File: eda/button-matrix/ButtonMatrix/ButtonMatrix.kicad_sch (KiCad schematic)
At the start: 50 parts, among them J1 Conn_01x12, J2 Conn_01x12

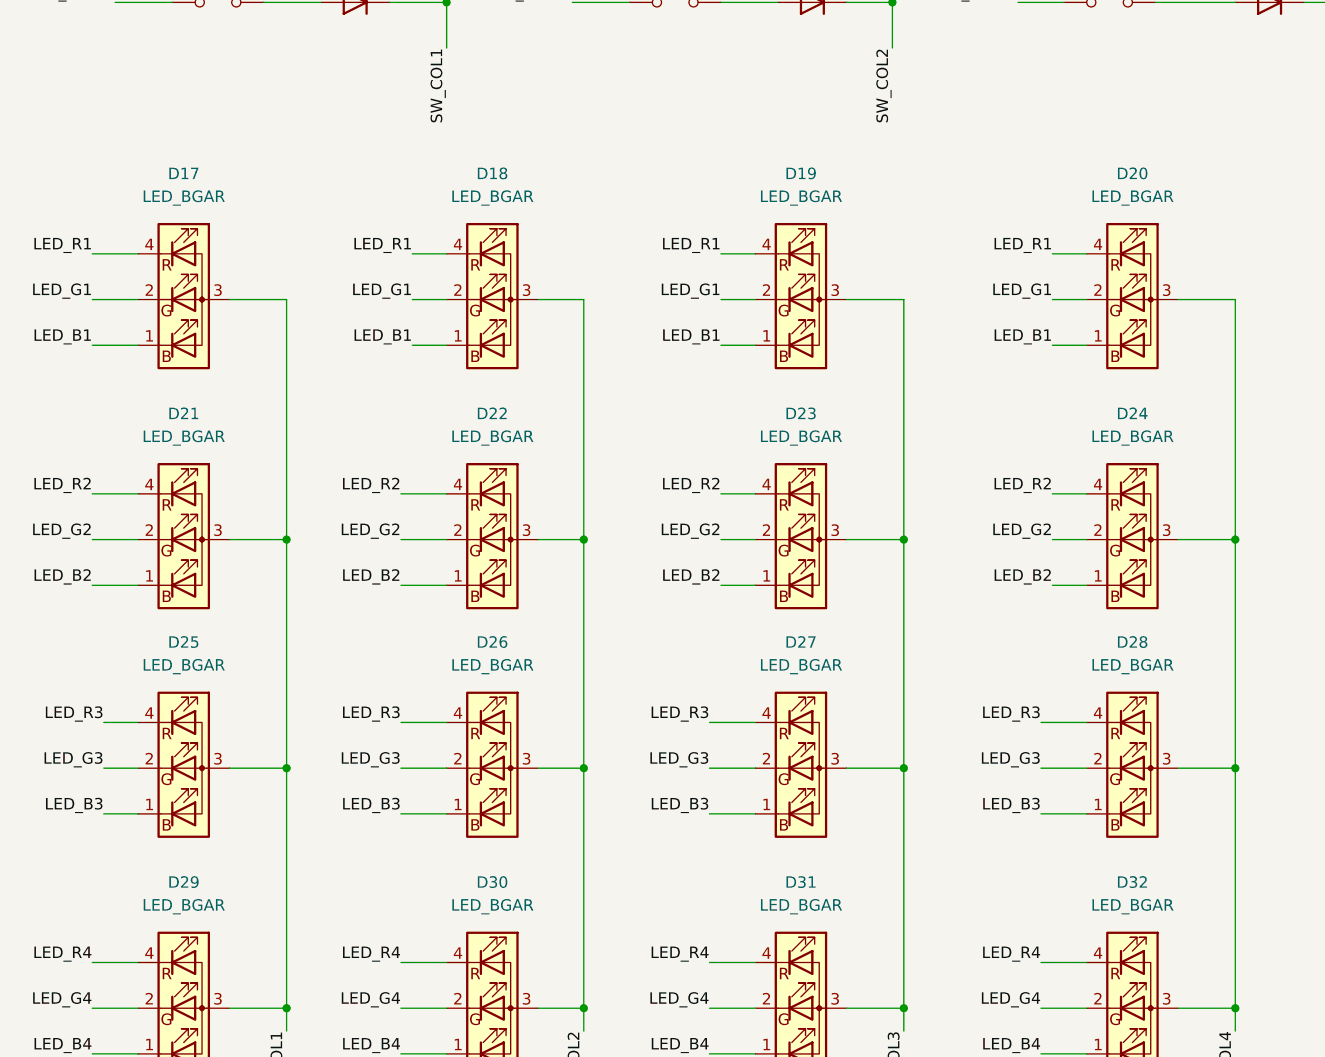
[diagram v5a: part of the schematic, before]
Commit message: - Fixed silk screen overlap issuess in button pcb
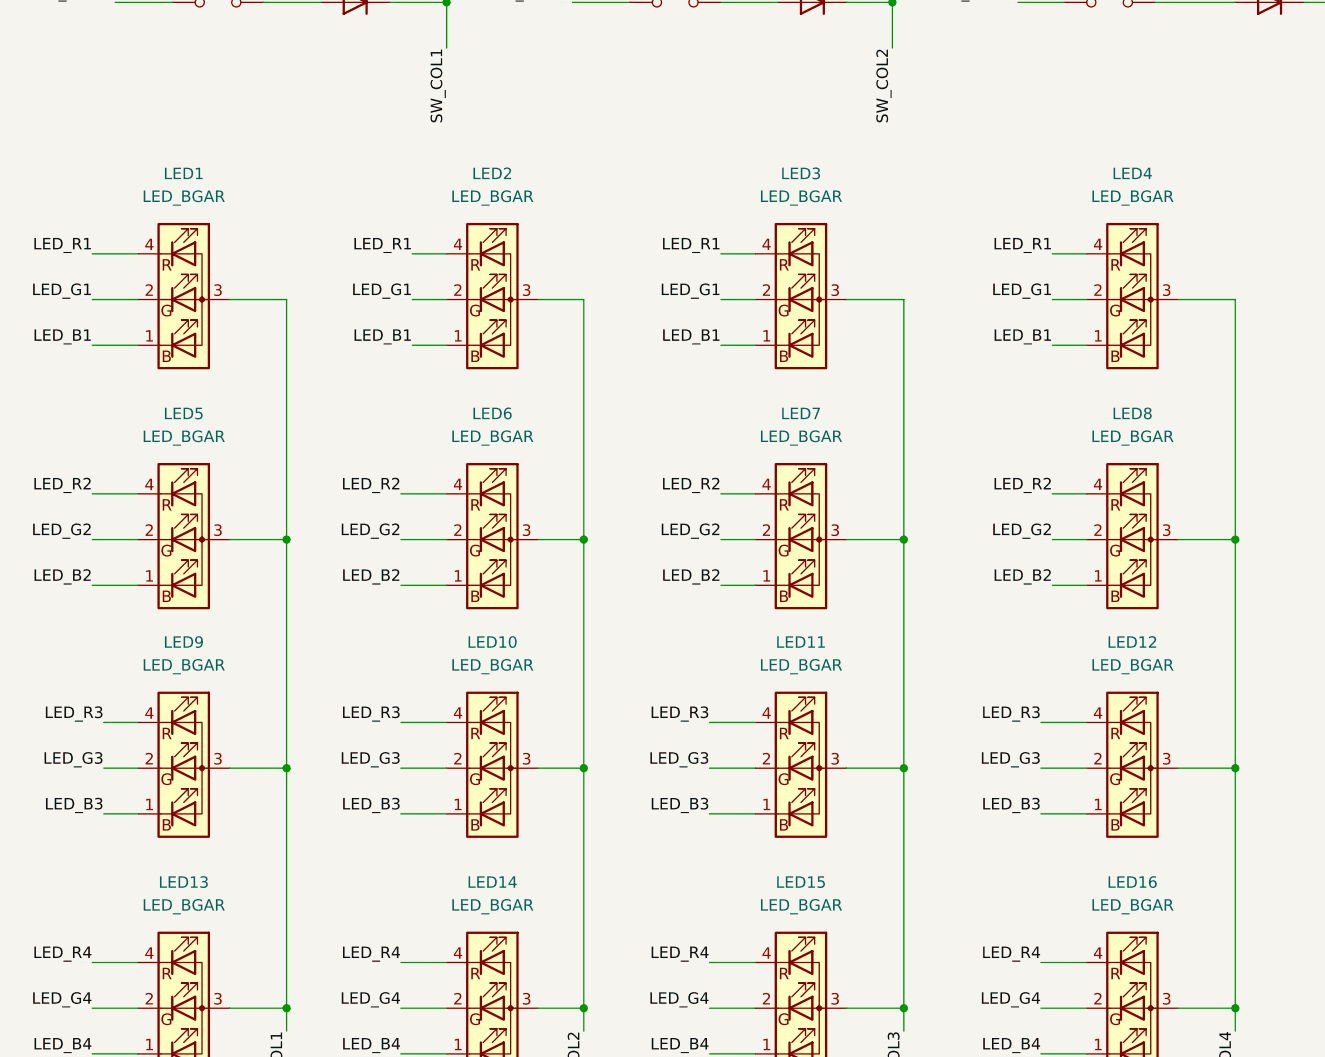
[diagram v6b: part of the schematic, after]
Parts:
- SW1, SW10, SW11, SW12, SW13, SW14, SW15, SW16, SW2, SW3, SW4, SW5, SW6, SW7, SW8, SW9: value (none) -> ~
- renumbered D17 to LED1, D26 to LED10, D27 to LED11, D28 to LED12, D29 to LED13, D30 to LED14, D31 to LED15, D32 to LED16, D18 to LED2, D19 to LED3, D20 to LED4, D21 to LED5, D22 to LED6, D23 to LED7, D24 to LED8, D25 to LED9
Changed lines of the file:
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@@
 		(dnp no)
 		(fields_autoplaced yes)
-		(property "Reference" "D22"
+		(property "Reference" "LED6"
 			(at 74.93 118.11 0)
 			(effects
@@
 			(project "ButtonMatrix"
 				(path "/a9cc6e02-ad1b-41d7-8cd8-8cf0c6fe637e"
-					(reference "D22")
+					(reference "LED6")
 					(unit 1)
 				)
@@
 		(on_board yes)
 		(dnp no)
-		(property "Reference" "D25"
+		(property "Reference" "LED9"
 			(at 40.64 143.51 0)
 			(effects
@@
 			(project "ButtonMatrix"
 				(path "/a9cc6e02-ad1b-41d7-8cd8-8cf0c6fe637e"
-					(reference "D25")
+					(reference "LED9")
 					(unit 1)
 				)
@@
 		(dnp no)
 		(fields_autoplaced yes)
-		(property "Reference" "D24"
+		(property "Reference" "LED8"
 			(at 146.05 118.11 0)
 			(effects
@@
 			(project "ButtonMatrix"
 				(path "/a9cc6e02-ad1b-41d7-8cd8-8cf0c6fe637e"
-					(reference "D24")
+					(reference "LED8")
 					(unit 1)
 				)
@@
 		(on_board yes)
 		(dnp no)
-		(property "Reference" "D27"
+		(property "Reference" "LED11"
 			(at 109.22 143.51 0)
 			(effects
@@
 			(project "ButtonMatrix"
 				(path "/a9cc6e02-ad1b-41d7-8cd8-8cf0c6fe637e"
-					(reference "D27")
+					(reference "LED11")
 					(unit 1)
 				)
@@
 			)
 		)
-		(property "Value" ""
+		(property "Value" "~"
 			(at 95.25 67.31 0)
 			(effects
@@
 			)
 		)
-		(property "Value" ""
+		(property "Value" "~"
 			(at 143.51 67.31 0)
 			(effects
@@
 		(dnp no)
 		(fields_autoplaced yes)
-		(property "Reference" "D17"
+		(property "Reference" "LED1"
 			(at 40.64 91.44 0)
 			(effects
@@
 			(project "ButtonMatrix"
 				(path "/a9cc6e02-ad1b-41d7-8cd8-8cf0c6fe637e"
-					(reference "D17")
+					(reference "LED1")
 					(unit 1)
 				)
@@
 		(dnp no)
 		(fields_autoplaced yes)
-		(property "Reference" "D18"
+		(property "Reference" "LED2"
 			(at 74.93 91.44 0)
 			(effects
@@
 			(project "ButtonMatrix"
 				(path "/a9cc6e02-ad1b-41d7-8cd8-8cf0c6fe637e"
-					(reference "D18")
+					(reference "LED2")
 					(unit 1)
 				)
@@
 			)
 		)
-		(property "Value" ""
+		(property "Value" "~"
 			(at 95.25 19.05 0)
 			(effects
@@
 			)
 		)
-		(property "Value" ""
+		(property "Value" "~"
 			(at 198.12 19.05 0)
 			(effects
@@
 			)
 		)
-		(property "Value" ""
+		(property "Value" "~"
 			(at 44.45 67.31 0)
 			(effects
@@
 			)
 		)
-		(property "Value" ""
+		(property "Value" "~"
 			(at 44.45 19.05 0)
 			(effects
@@
 			)
 		)
-		(property "Value" ""
+		(property "Value" "~"
 			(at 198.12 50.8 0)
 			(effects
@@
 			)
 		)
-		(property "Value" ""
+		(property "Value" "~"
 			(at 198.12 35.56 0)
 			(effects
@@
 			)
 		)
-		(property "Value" ""
+		(property "Value" "~"
 			(at 143.51 35.56 0)
 			(effects
@@
 		(on_board yes)
 		(dnp no)
-		(property "Reference" "D30"
+		(property "Reference" "LED14"
 			(at 74.93 170.18 0)
 			(effects
@@
 			(project "ButtonMatrix"
 				(path "/a9cc6e02-ad1b-41d7-8cd8-8cf0c6fe637e"
-					(reference "D30")
+					(reference "LED14")
 					(unit 1)
 				)
@@
 		(on_board yes)
 		(dnp no)
-		(property "Reference" "D26"
+		(property "Reference" "LED10"
 			(at 74.93 143.51 0)
 			(effects
@@
 			(project "ButtonMatrix"
 				(path "/a9cc6e02-ad1b-41d7-8cd8-8cf0c6fe637e"
-					(reference "D26")
+					(reference "LED10")
 					(unit 1)
 				)
@@
 			)
 		)
-		(property "Value" ""
+		(property "Value" "~"
 			(at 198.12 67.31 0)
 			(effects
@@
 			)
 		)
-		(property "Value" ""
+		(property "Value" "~"
 			(at 95.25 50.8 0)
 			(effects
@@
 			)
 		)
-		(property "Value" ""
+		(property "Value" "~"
 			(at 44.45 35.56 0)
 			(effects
@@
 			)
 		)
-		(property "Value" ""
+		(property "Value" "~"
 			(at 95.25 35.56 0)
 			(effects
@@
 			)
 		)
-		(property "Value" ""
+		(property "Value" "~"
 			(at 143.51 19.05 0)
 			(effects
@@
 		(dnp no)
 		(fields_autoplaced yes)
-		(property "Reference" "D19"
+		(property "Reference" "LED3"
 			(at 109.22 91.44 0)
 			(effects
@@
 			(project "ButtonMatrix"
 				(path "/a9cc6e02-ad1b-41d7-8cd8-8cf0c6fe637e"
-					(reference "D19")
+					(reference "LED3")
 					(unit 1)
 				)
@@
 		(dnp no)
 		(fields_autoplaced yes)
-		(property "Reference" "D20"
+		(property "Reference" "LED4"
 			(at 146.05 91.44 0)
 			(effects
@@
 			(project "ButtonMatrix"
 				(path "/a9cc6e02-ad1b-41d7-8cd8-8cf0c6fe637e"
-					(reference "D20")
+					(reference "LED4")
 					(unit 1)
 				)
@@
 		(dnp no)
 		(fields_autoplaced yes)
-		(property "Reference" "D23"
+		(property "Reference" "LED7"
 			(at 109.22 118.11 0)
 			(effects
@@
 			(project "ButtonMatrix"
 				(path "/a9cc6e02-ad1b-41d7-8cd8-8cf0c6fe637e"
-					(reference "D23")
+					(reference "LED7")
 					(unit 1)
 				)
@@
 		(on_board yes)
 		(dnp no)
-		(property "Reference" "D32"
+		(property "Reference" "LED16"
 			(at 146.05 170.18 0)
 			(effects
@@
 			(project "ButtonMatrix"
 				(path "/a9cc6e02-ad1b-41d7-8cd8-8cf0c6fe637e"
-					(reference "D32")
+					(reference "LED16")
 					(unit 1)
 				)
@@
 			)
 		)
-		(property "Value" ""
+		(property "Value" "~"
 			(at 44.45 50.8 0)
 			(effects
@@
 		(on_board yes)
 		(dnp no)
-		(property "Reference" "D28"
+		(property "Reference" "LED12"
 			(at 146.05 143.51 0)
 			(effects
@@
 			(project "ButtonMatrix"
 				(path "/a9cc6e02-ad1b-41d7-8cd8-8cf0c6fe637e"
-					(reference "D28")
+					(reference "LED12")
 					(unit 1)
 				)
@@
 		(on_board yes)
 		(dnp no)
-		(property "Reference" "D29"
+		(property "Reference" "LED13"
 			(at 40.64 170.18 0)
 			(effects
@@
 			(project "ButtonMatrix"
 				(path "/a9cc6e02-ad1b-41d7-8cd8-8cf0c6fe637e"
-					(reference "D29")
+					(reference "LED13")
 					(unit 1)
 				)
@@
 			)
 		)
-		(property "Value" ""
+		(property "Value" "~"
 			(at 143.51 50.8 0)
 			(effects
@@
 		(on_board yes)
 		(dnp no)
-		(property "Reference" "D31"
+		(property "Reference" "LED15"
 			(at 109.22 170.18 0)
 			(effects
@@
 			(project "ButtonMatrix"
 				(path "/a9cc6e02-ad1b-41d7-8cd8-8cf0c6fe637e"
-					(reference "D31")
+					(reference "LED15")
 					(unit 1)
 				)
@@
 		(dnp no)
 		(fields_autoplaced yes)
-		(property "Reference" "D21"
+		(property "Reference" "LED5"
 			(at 40.64 118.11 0)
 			(effects
@@
 			(project "ButtonMatrix"
 				(path "/a9cc6e02-ad1b-41d7-8cd8-8cf0c6fe637e"
-					(reference "D21")
+					(reference "LED5")
 					(unit 1)
 				)
